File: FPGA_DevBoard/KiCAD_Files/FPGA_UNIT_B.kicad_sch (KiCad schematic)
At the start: 81 parts, among them J15 6130XX11121_61301611121, J16 6130XX11121_61301611121, J7 L77HDE15SD1CH4F, U19 XC7S50-1FTGB196C, U21 USBLC6-2SC6, U22 USBLC6-2SC6, U23 USBLC6-2SC6, U24 USBLC6-2SC6, U25 USBLC6-2SC6, U26 USBLC6-2SC6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

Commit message: Final updates
Draft 1 Finished!
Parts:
- added R66: 1k, Resistor_SMD:R_0805_2012Metric, symbol Device:R_US
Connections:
- net +3V3: now also R26.1; no longer R26.2
- net GND: now also R66.2
- net at U19.B10 (IO_L3P_T0_DQS_PUDC_B_14): now also R26.2, R66.1; no longer R26.1
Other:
- moved on the sheet: R26
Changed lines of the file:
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@@
 	)
 	(junction
+		(at 66.04 118.11)
+		(diameter 0)
+		(color 0 0 0 0)
+	)
+	(junction
 		(at 44.45 100.33)
 		(diameter 0)
@@
 	(wire
 		(pts
+			(xy 66.04 116.84) (xy 66.04 118.11)
+		)
+		(stroke
+			(width 0)
+			(type default)
+		)
+	)
+	(wire
+		(pts
 			(xy 372.11 146.05) (xy 359.41 146.05)
 		)
@@
 	(wire
 		(pts
-			(xy 68.58 111.76) (xy 68.58 118.11)
-		)
-		(stroke
-			(width 0)
-			(type default)
-		)
-	)
-	(wire
-		(pts
 			(xy 388.62 194.31) (xy 401.32 194.31)
 		)
@@
 	(wire
 		(pts
-			(xy 80.01 118.11) (xy 83.82 118.11)
-		)
-		(stroke
-			(width 0)
-			(type default)
-		)
-	)
-	(wire
-		(pts
 			(xy 269.24 121.92) (xy 287.02 121.92)
 		)
@@
 	(wire
 		(pts
+			(xy 66.04 118.11) (xy 83.82 118.11)
+		)
+		(stroke
+			(width 0)
+			(type default)
+		)
+	)
+	(wire
+		(pts
 			(xy 26.67 190.5) (xy 27.94 190.5)
 		)
@@
 	(wire
 		(pts
+			(xy 66.04 106.68) (xy 66.04 109.22)
+		)
+		(stroke
+			(width 0)
+			(type default)
+		)
+	)
+	(wire
+		(pts
 			(xy 269.24 111.76) (xy 287.02 111.76)
 		)
@@
 	(wire
 		(pts
-			(xy 72.39 118.11) (xy 68.58 118.11)
-		)
-		(stroke
-			(width 0)
-			(type default)
-		)
-	)
-	(wire
-		(pts
 			(xy 240.03 76.2) (xy 252.73 76.2)
 		)
@@
 		)
 	)
+	(label "VCCO_14"
+		(at 66.04 106.68 0)
+		(effects
+			(font
+				(size 1.27 1.27)
+			)
+			(justify left bottom)
+		)
+	)
 	(label "GPIO_OUT_27"
 		(at 359.41 214.63 0)
@@
 	(symbol
 		(lib_id "Device:R_US")
-		(at 76.2 118.11 270)
+		(at 66.04 113.03 0)
 		(unit 1)
 		(exclude_from_sim no)
@@
 		(dnp no)
 		(property "Reference" "R26"
-			(at 72.136 119.126 90)
+			(at 68.326 113.284 90)
 			(effects
 				(font
@@
 		)
 		(property "Value" "1k"
-			(at 81.28 119.126 90)
+			(at 67.056 107.95 90)
 			(effects
 				(font
@@
 		)
 		(property "Footprint" "Resistor_SMD:R_0402_1005Metric"
-			(at 75.946 119.126 90)
+			(at 67.056 113.284 90)
 			(effects
 				(font
@@
 		)
 		(property "Datasheet" "~"
-			(at 76.2 118.11 0)
+			(at 66.04 113.03 0)
 			(effects
 				(font
@@
 		)
 		(property "Description" "Resistor, US symbol"
-			(at 76.2 118.11 0)
+			(at 66.04 113.03 0)
 			(effects
 				(font
@@
 	)
 	(symbol
-		(lib_id "power:+3V3")
-		(at 68.58 111.76 0)
-		(unit 1)
-		(exclude_from_sim no)
-		(in_bom yes)
-		(on_board yes)
-		(dnp no)
-		(fields_autoplaced yes)
-		(property "Reference" "#PWR021"
-			(at 68.58 115.57 0)
-			(effects
-				(font
-					(size 1.27 1.27)
-				)
-				(hide yes)
-			)
-		)
-		(property "Value" "+3V3"
-			(at 68.58 106.68 0)
-			(effects
-				(font
-					(size 1.27 1.27)
-				)
-			)
-		)
-		(property "Footprint" ""
-			(at 68.58 111.76 0)
-			(effects
-				(font
-					(size 1.27 1.27)
-				)
-				(hide yes)
-			)
-		)
-		(property "Datasheet" ""
-			(at 68.58 111.76 0)
-			(effects
-				(font
-					(size 1.27 1.27)
-				)
-				(hide yes)
-			)
-		)
-		(property "Description" "Power symbol creates a global label with name \"+3V3\""
-			(at 68.58 111.76 0)
-			(effects
-				(font
-					(size 1.27 1.27)
-				)
-				(hide yes)
-			)
-		)
-		(pin "1"
-		)
-		(instances
-			(project "FPGA_DevBoard"
-				(path "/29dacc10-fb0d-42da-8b4b-fe903faf3f1a/9f3372dd-c4cd-4e98-a06a-d48a7fd00c4b"
-					(reference "#PWR021")
-					(unit 1)
-				)
-			)
-		)
-	)
-	(symbol
 		(lib_id "Device:R_US")
 		(at 290.83 142.24 90)
@@
 	)
 	(symbol
+		(lib_id "power:GND")
+		(at 66.04 125.73 0)
+		(unit 1)
+		(exclude_from_sim no)
+		(in_bom yes)
+		(on_board yes)
+		(dnp no)
+		(fields_autoplaced yes)
+		(property "Reference" "#PWR021"
+			(at 66.04 132.08 0)
+			(effects
+				(font
+					(size 1.27 1.27)
+				)
+				(hide yes)
+			)
+		)
+		(property "Value" "GND"
+			(at 66.04 130.81 0)
+			(effects
+				(font
+					(size 1.27 1.27)
+				)
+			)
+		)
+		(property "Footprint" ""
+			(at 66.04 125.73 0)
+			(effects
+				(font
+					(size 1.27 1.27)
+				)
+				(hide yes)
+			)
+		)
+		(property "Datasheet" ""
+			(at 66.04 125.73 0)
+			(effects
+				(font
+					(size 1.27 1.27)
+				)
+				(hide yes)
+			)
+		)
+		(property "Description" "Power symbol creates a global label with name \"GND\" , ground"
+			(at 66.04 125.73 0)
+			(effects
+				(font
+					(size 1.27 1.27)
+				)
+				(hide yes)
+			)
+		)
+		(pin "1"
+		)
+		(instances
+			(project "FPGA_DevBoard"
+				(path "/29dacc10-fb0d-42da-8b4b-fe903faf3f1a/9f3372dd-c4cd-4e98-a06a-d48a7fd00c4b"
+					(reference "#PWR021")
+					(unit 1)
+				)
+			)
+		)
+	)
+	(symbol
 		(lib_id "Device:R_US")
 		(at 44.45 96.52 0)
@@
 					(unit 1)
 				)
+			)
+		)
+	)
+	(symbol
+		(lib_id "Device:R_US")
+		(at 66.04 121.92 0)
+		(unit 1)
+		(exclude_from_sim no)
+		(in_bom yes)
+		(on_board yes)
+		(dnp no)
+		(property "Reference" "R66"
+			(at 68.326 122.174 90)
+			(effects
+				(font
+					(size 1.27 1.27)
+				)
+			)
+		)
+		(property "Value" "1k"
+			(at 63.754 122.428 90)
+			(effects
+				(font
+					(size 1.27 1.27)
+				)
+			)
+		)
+		(property "Footprint" "Resistor_SMD:R_0805_2012Metric"
+			(at 67.056 122.174 90)
+			(effects
+				(font
+					(size 1.27 1.27)
+				)
+				(hide yes)
+			)
+		)
+		(property "Datasheet" "~"
+			(at 66.04 121.92 0)
+			(effects
+				(font
+					(size 1.27 1.27)
+				)
+				(hide yes)
+			)
+		)
+		(property "Description" "Resistor, US symbol"
+			(at 66.04 121.92 0)
+			(effects
+				(font
+					(size 1.27 1.27)
+				)
+				(hide yes)
+			)
+		)
+		(pin "1"
+		)
+		(pin "2"
+		)
+		(instances
+			(project "FPGA_DevBoard"
+				(path "/29dacc10-fb0d-42da-8b4b-fe903faf3f1a/9f3372dd-c4cd-4e98-a06a-d48a7fd00c4b"
+					(reference "R66")
+					(unit 1)
+				)

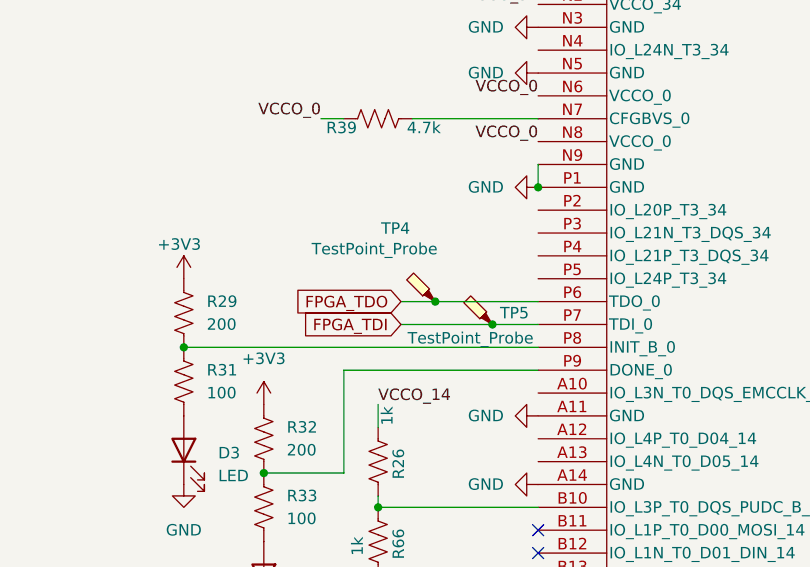
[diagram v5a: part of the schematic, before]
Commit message: Updated the NBSB IO to not go to input only, need to change this on the layout. Updated the FPGA clk to go to a positive differential signal with MCRR - need to change on layout. Updated the USB-UART bridge to not have Regin grounded - need to change on layout.
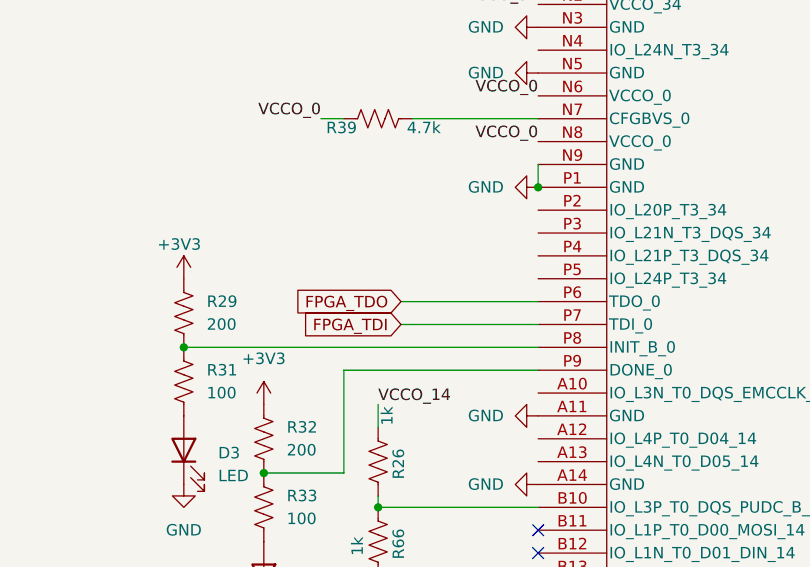
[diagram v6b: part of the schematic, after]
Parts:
- removed TP4, TP5: TestPoint_Probe, TestPoint:TestPoint_Pad_D1.0mm, symbol Connector:TestPoint_Probe

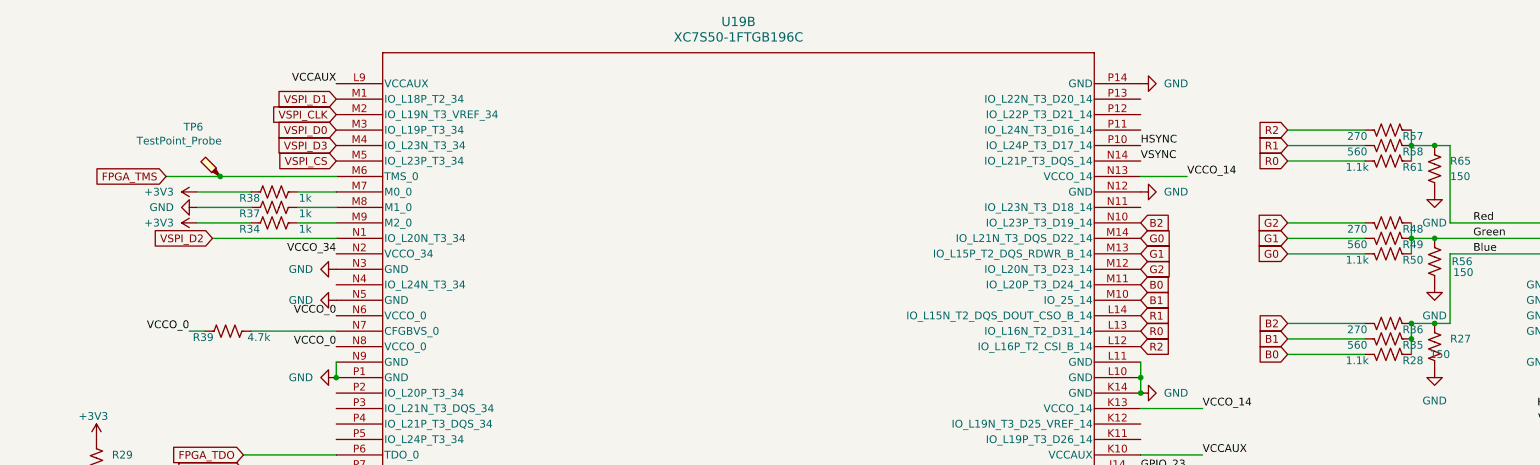
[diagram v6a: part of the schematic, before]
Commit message: OK I PULL UP
Added pull up resistors to SPI CS, pull down to GPIO12, redid vga bus lines. This also might include the FPGA clock being correct? Idk if that was committed before
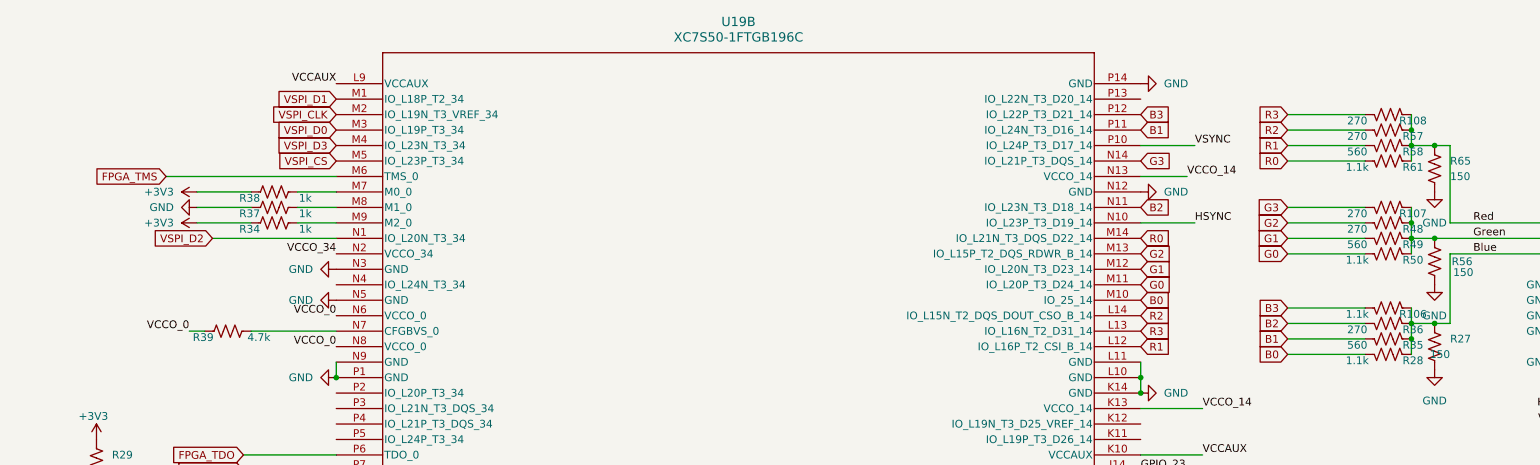
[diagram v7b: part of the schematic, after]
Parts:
- removed TP6: TestPoint_Probe, TestPoint:TestPoint_Pad_D1.0mm, symbol Connector:TestPoint_Probe
- added R106: 1.1k, Resistor_SMD:R_0402_1005Metric, symbol Device:R_US
- added R107, R108: 270, Resistor_SMD:R_0402_1005Metric, symbol Device:R_US
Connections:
- net B0: now also U19.M10 (IO_25_14); no longer U19.M11 (IO_L20P_T3_D24_14)
- net B1: now also U19.P11 (IO_L24N_T3_D16_14); no longer U19.M10 (IO_25_14)
- net B2: now also U19.N11 (IO_L23N_T3_D18_14); no longer U19.N10 (IO_L23P_T3_D19_14)
- net Blue: now also R106.2
- net G0: now also U19.M11 (IO_L20P_T3_D24_14); no longer U19.M14 (IO_L21N_T3_DQS_D22_14)
- net G1: now also U19.M12 (IO_L20N_T3_D23_14); no longer U19.M13 (IO_L15P_T2_DQS_RDWR_B_14)
- net G2: now also U19.M13 (IO_L15P_T2_DQS_RDWR_B_14); no longer U19.M12 (IO_L20N_T3_D23_14)
- net Green: now also R107.2
- net HSYNC: now also U19.N10 (IO_L23P_T3_D19_14); no longer U19.P10 (IO_L24P_T3_D17_14)
- net R0: now also U19.M14 (IO_L21N_T3_DQS_D22_14); no longer U19.L13 (IO_L16N_T2_D31_14)
- net R1: now also U19.L12 (IO_L16P_T2_CSI_B_14); no longer U19.L14 (IO_L15N_T2_DQS_DOUT_CSO_B_14)
- net R2: now also U19.L14 (IO_L15N_T2_DQS_DOUT_CSO_B_14); no longer U19.L12 (IO_L16P_T2_CSI_B_14)
- net Red: now also R108.2
- net VSYNC: now also U19.P10 (IO_L24P_T3_D17_14); no longer U19.N14 (IO_L21P_T3_DQS_14)
- net B3: now reaches U19.P12 (IO_L22P_T3_D21_14)
- net B3: now also R106.1
- new net G3: R107.1, U19.N14 (IO_L21P_T3_DQS_14)
- new net R3: R108.1, U19.L13 (IO_L16N_T2_D31_14)

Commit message: Final Final Final Lol
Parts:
- R106: value 1.1k -> 270
- R28, R50, R61: value 1.1k -> 2.2k
- R35, R49, R58: value 560 -> 1.1k
- R36, R48, R57: value 270 -> 560
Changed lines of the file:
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@@
 			)
 		)
-		(property "Value" "1.1k"
+		(property "Value" "2.2k"
 			(at 251.46 48.006 90)
 			(show_name no)
@@
 			)
 		)
-		(property "Value" "1.1k"
+		(property "Value" "2.2k"
 			(at 251.46 79.756 90)
 			(show_name no)
@@
 			)
 		)
-		(property "Value" "560"
+		(property "Value" "1.1k"
 			(at 251.46 77.216 90)
 			(show_name no)
@@
 			)
 		)
-		(property "Value" "270"
+		(property "Value" "560"
 			(at 251.46 42.926 90)
 			(show_name no)
@@
 			)
 		)
-		(property "Value" "1.1k"
+		(property "Value" "270"
 			(at 251.46 72.136 90)
 			(show_name no)
@@
 			)
 		)
-		(property "Value" "1.1k"
+		(property "Value" "2.2k"
 			(at 251.46 63.246 90)
 			(show_name no)
@@
 			)
 		)
-		(property "Value" "270"
+		(property "Value" "560"
 			(at 251.46 58.166 90)
 			(show_name no)
@@
 			)
 		)
-		(property "Value" "270"
+		(property "Value" "560"
 			(at 251.46 74.676 90)
 			(show_name no)
@@
 			)
 		)
-		(property "Value" "560"
+		(property "Value" "1.1k"
 			(at 251.46 45.466 90)
 			(show_name no)
@@
 			)
 		)
-		(property "Value" "560"
+		(property "Value" "1.1k"
 			(at 251.46 60.706 90)
 			(show_name no)
